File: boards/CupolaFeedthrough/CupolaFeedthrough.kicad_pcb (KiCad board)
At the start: 2 copper layers, 165.5 x 91.8 mm, 22 parts, among them J101 CONN_01X15, J102 CONN_01X15, J103 CONN_01X15, J104 DB15_FEMALE, J105 DB15_FEMALE, J106 DB15_FEMALE, J107 GND, J108 GND, J109 GND, J110 GND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

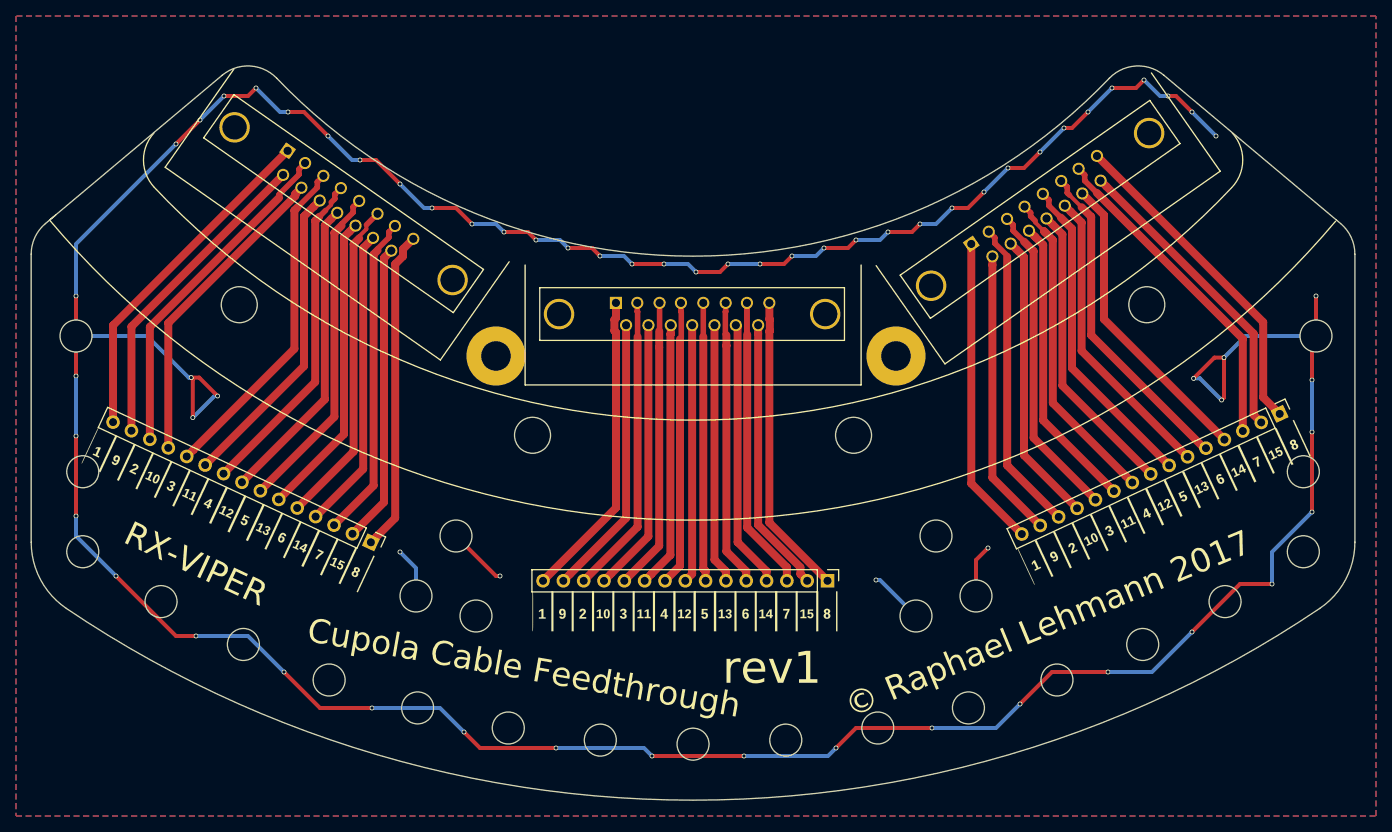
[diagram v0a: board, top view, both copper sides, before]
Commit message: [CupolaFeedthrough] fix board outline
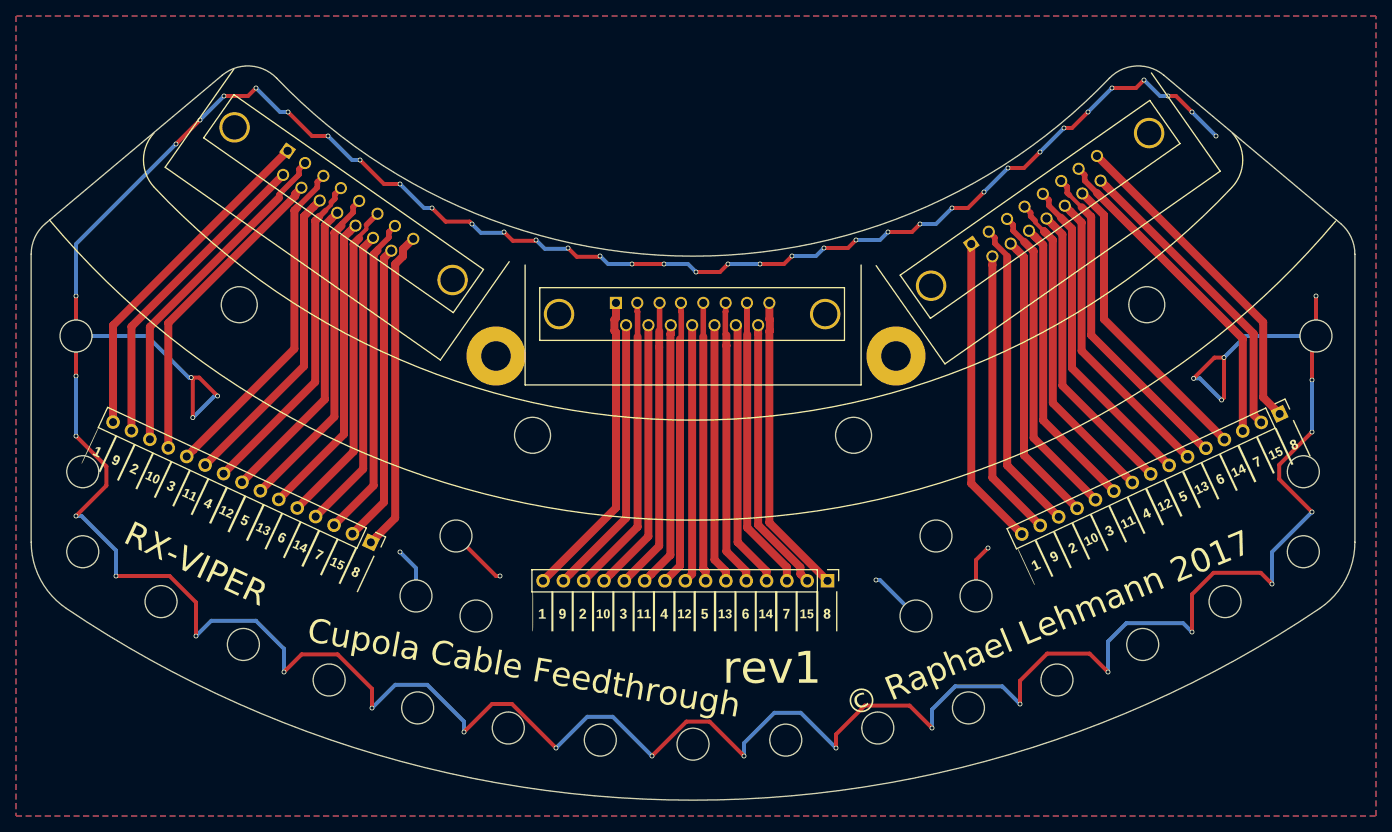
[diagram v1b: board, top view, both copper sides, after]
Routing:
- net GND: track 507.5 -> 558.4 mm
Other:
- outline, holes or cut-outs redrawn
